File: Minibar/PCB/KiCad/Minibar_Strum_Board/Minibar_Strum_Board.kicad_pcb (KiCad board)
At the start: 2 copper layers, 160.3 x 29 mm, 24 parts, among them U1 ProMicro

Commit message: Updated Minibar strum board
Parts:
- removed ? (x13): , 
- added J1: Conn_01x09_Pin, Connector_PinHeader_2.54mm:PinHeader_1x09_P2.54mm_Vertical, F.Cu at (48.4, 104.8)
- added J2: Conn_01x02_Pin, Connector_PinHeader_2.54mm:PinHeader_1x02_P2.54mm_Vertical, F.Cu at (166.6, 109.2)
- added J4: Conn_01x02_Pin, Connector_PinHeader_2.54mm:PinHeader_1x02_P2.54mm_Vertical, F.Cu at (166.7, 118.0)
- D1: renamed from D5; value strum_down_led -> led_strum_down; footprint Controller_Inputs:LED_RGB_5050_DOTSTAR -> LED_SMD:LED_RGB_5050-6
- D2: renamed from D5; value strum_up_led -> led_strum_up; footprint Controller_Inputs:LED_RGB_5050_DOTSTAR -> LED_SMD:LED_RGB_5050-6
- D3, D4: renamed from D5; footprint Controller_Inputs:LED_RGB_5050_DOTSTAR -> LED_SMD:LED_RGB_5050-6
- J3: renamed from SINGLE TILT JUMPER; value SolderJumper-2_P1.3mm_Open_Pad1.0x1.5mm -> Conn_01x02_Pin; footprint Jumper:SolderJumper-2_P1.3mm_Open_Pad1.0x1.5mm -> Minibar:Solder_Jumper
- SW1, SW2: renamed from  ; footprint marbastlib-mx:SW_MX_HS_1u -> Minibar:Kailh_Hotswap_MX; moved to F.Cu
- SW3, SW4: renamed from REF**; value SW_SPST_PTS645 -> SW
- U1: value ProMicro -> KB2040; footprint Controller_Inputs:KB2040-ProMicroPins -> Minibar:KB2040-SMD
- U2: renamed from U**; value RKJXV1224005 -> Joystick; footprint Controller_Inputs:RKJXV1224005 -> Minibar:Joystick
- turned SW1 to 0 degrees
- turned SW2 to 180 degrees
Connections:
- D1 pad 5: Net-(D4-C0) -> fret_sck
- D1 pad 6: Net-(D4-D0) -> fret_mosi
- J3 pad 2: Tilt -> Tilt 2
- SW1 pad : GND -> (no net)
- SW1 pad 2: Down -> GND
- SW2 pad : GND -> (no net)
- SW2 pad 1: GND -> Up
- U1 pad 1: (no net) -> unconnected-(U1-TX0/PD3-Pad1)
- U1 pad 2: (no net) -> unconnected-(U1-RX1/PD2-Pad2)
- U1 pad 20: (no net) -> unconnected-(U1-A3/PF4-Pad20)
- U1 pad 22: (no net) -> unconnected-(U1-RST-Pad22)
- U1 pad 24: (no net) -> unconnected-(U1-RAW-Pad24)
- U2 pad SH: SW -> unconnected-(U2-PadSH)
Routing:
- net VCC: track 225.0 -> 2.75 mm
- net Net-(D4-C0): track 78.3 -> 0.00 mm, vias 1 -> 0
- net Net-(D4-D0): track 76.9 -> 0.00 mm, vias 1 -> 0
- net fret_sck: track 0.00 -> 71.1 mm, vias 0 -> 1
- net fret_mosi: track 0.00 -> 69.7 mm, vias 0 -> 1
- net GND: track 0.00 -> 38.4 mm, vias 0 -> 3
- net Tilt: track 39.2 -> 26.0 mm
- net Tilt 2: track 0.00 -> 10.6 mm
- net VRY: track 145.2 -> 142.3 mm
- net Net-(D1-DI): track 24.6 -> 21.8 mm
- net Red: track 151.2 -> 148.6 mm
- net Green: track 152.7 -> 150.4 mm
- net Blue: track 149.4 -> 147.1 mm
- net Net-(D1-CI): track 24.6 -> 22.4 mm
- net Yellow: track 150.0 -> 147.8 mm
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- added copper zone on F.Cu, net VCC
- removed copper zone on F.Cu, net GND

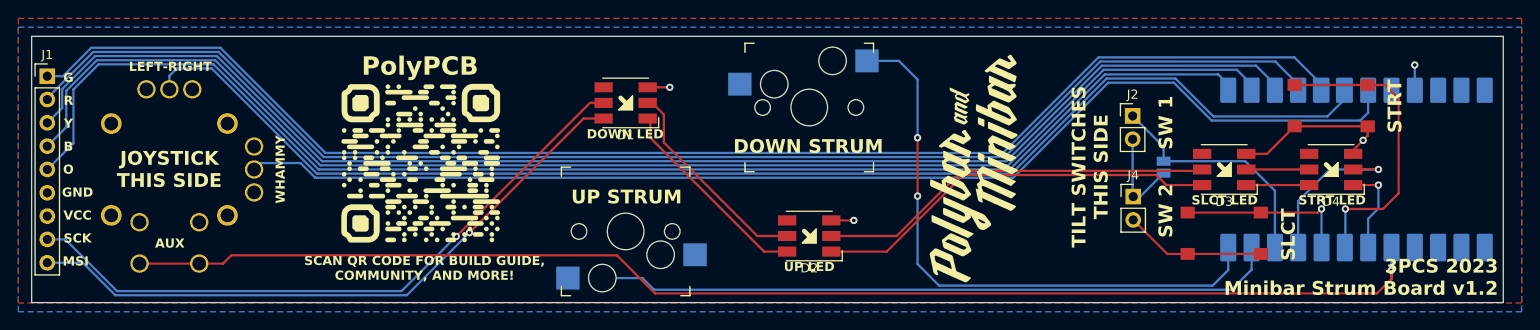
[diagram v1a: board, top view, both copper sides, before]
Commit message: Resolved all of the errors and most of the warnings
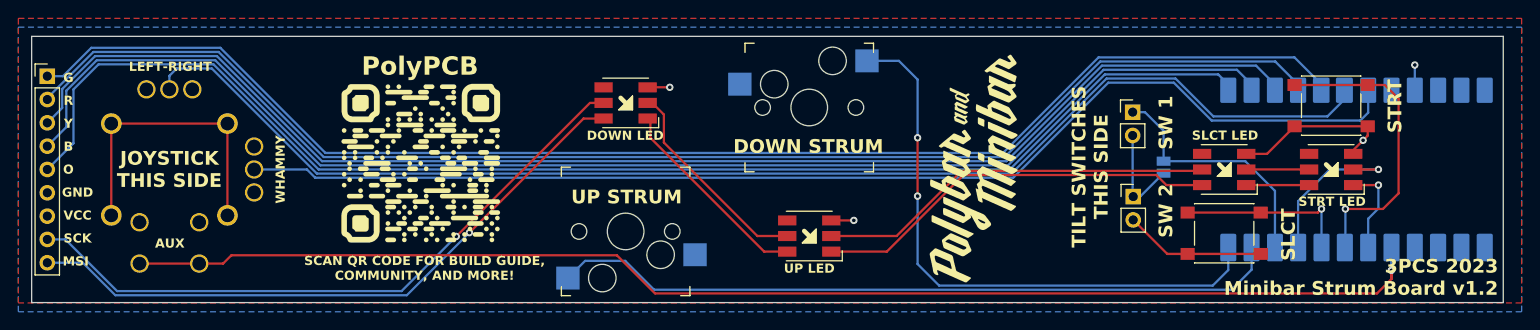
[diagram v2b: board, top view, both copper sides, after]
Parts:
- moved J2 0.41 mm to (166.6, 108.8)
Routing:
- net unconnected-(U2-PadSH): track 0.00 -> 32.7 mm
- net Up: track 73.8 -> 79.1 mm
- net Tilt: track 26.0 -> 27.2 mm
- net VRX: track 131.6 -> 130.5 mm
